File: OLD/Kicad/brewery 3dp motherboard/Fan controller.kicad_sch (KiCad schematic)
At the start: 6 parts, among them J28 jumpers, J29 JST-XH, U18 DOZ45N03T

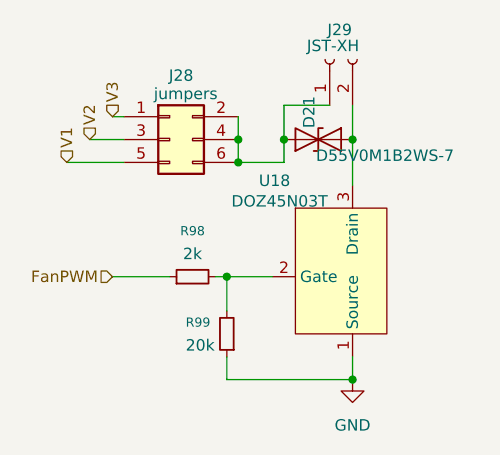
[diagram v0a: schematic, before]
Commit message: cleaned up structure a bit
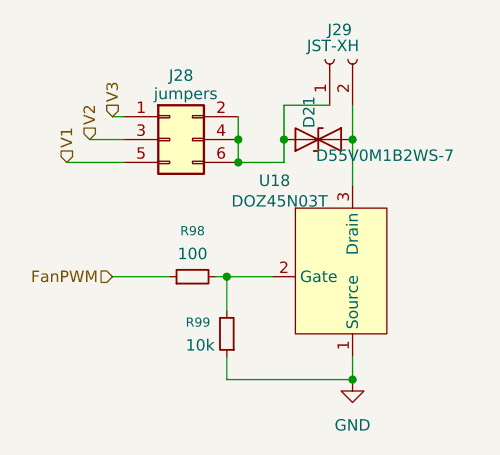
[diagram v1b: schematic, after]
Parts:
- R98: value 2k -> 100; footprint Resistor_SMD:R_0603_1608Metric -> Resistor_SMD:R_0402_1005Metric
- R99: value 20k -> 10k; footprint Resistor_SMD:R_0603_1608Metric -> Resistor_SMD:R_0402_1005Metric
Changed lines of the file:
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@@
 			)
 		)
-		(property "Value" "2k"
+		(property "Value" "100"
 			(at 100.33 68.58 90)
 			(show_name no)
@@
 			)
 		)
-		(property "Footprint" "Resistor_SMD:R_0603_1608Metric"
+		(property "Footprint" "Resistor_SMD:R_0402_1005Metric"
 			(at 100.33 71.12 0)
 			(hide yes)
@@
 			)
 		)
-		(property "Value" "20k"
+		(property "Value" "10k"
 			(at 99.568 78.74 0)
 			(show_name no)
@@
 			)
 		)
-		(property "Footprint" "Resistor_SMD:R_0603_1608Metric"
+		(property "Footprint" "Resistor_SMD:R_0402_1005Metric"
 			(at 104.14 77.47 0)
 			(hide yes)
